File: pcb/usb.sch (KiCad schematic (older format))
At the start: 1 part

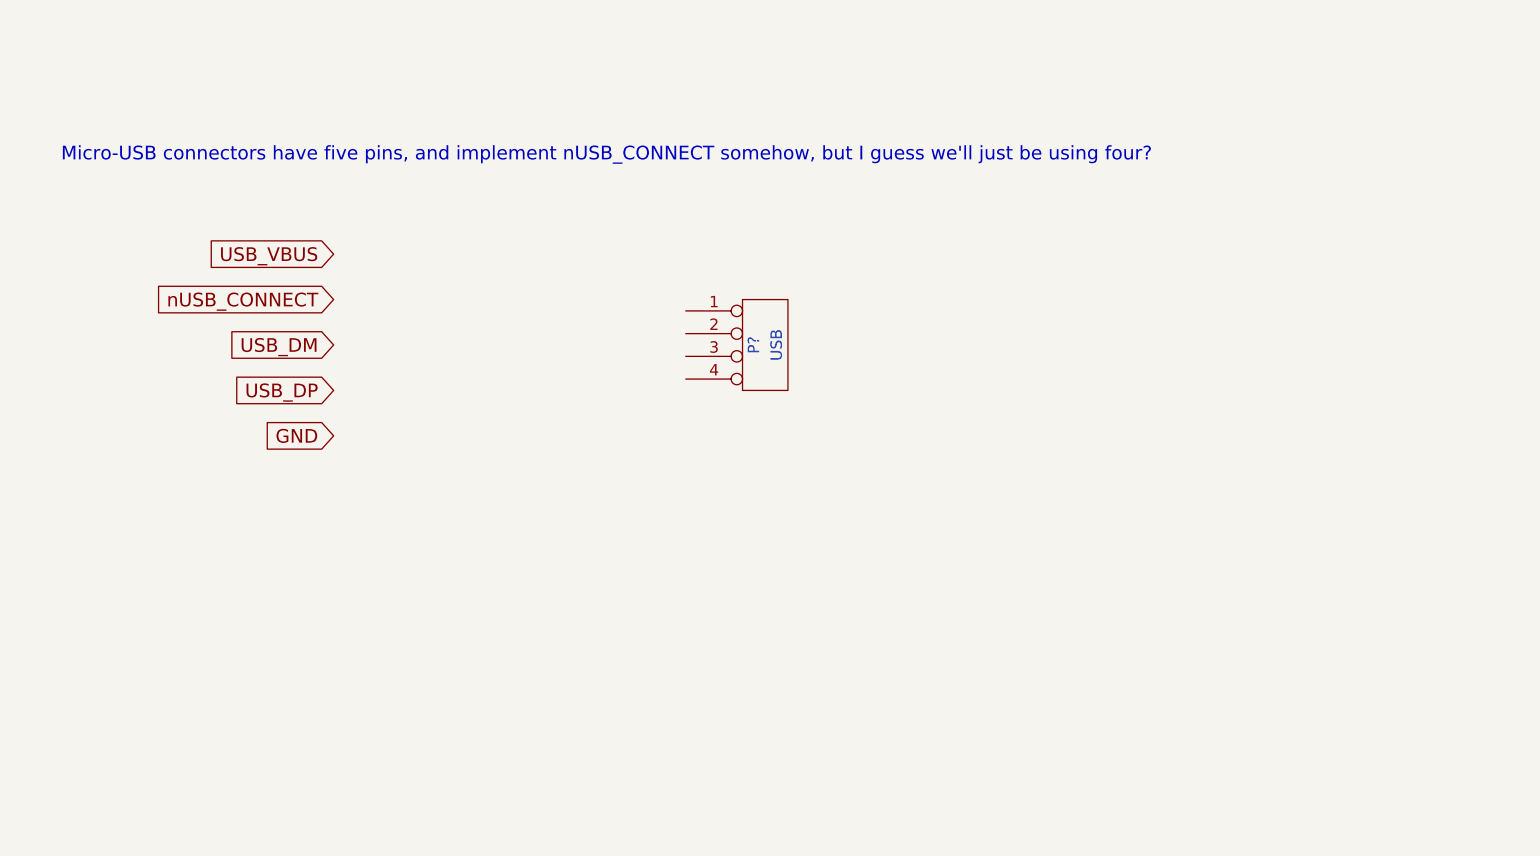
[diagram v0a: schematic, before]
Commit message: added reset pullup, some caps, usb resistors, explanation for nUSB_CONNECT
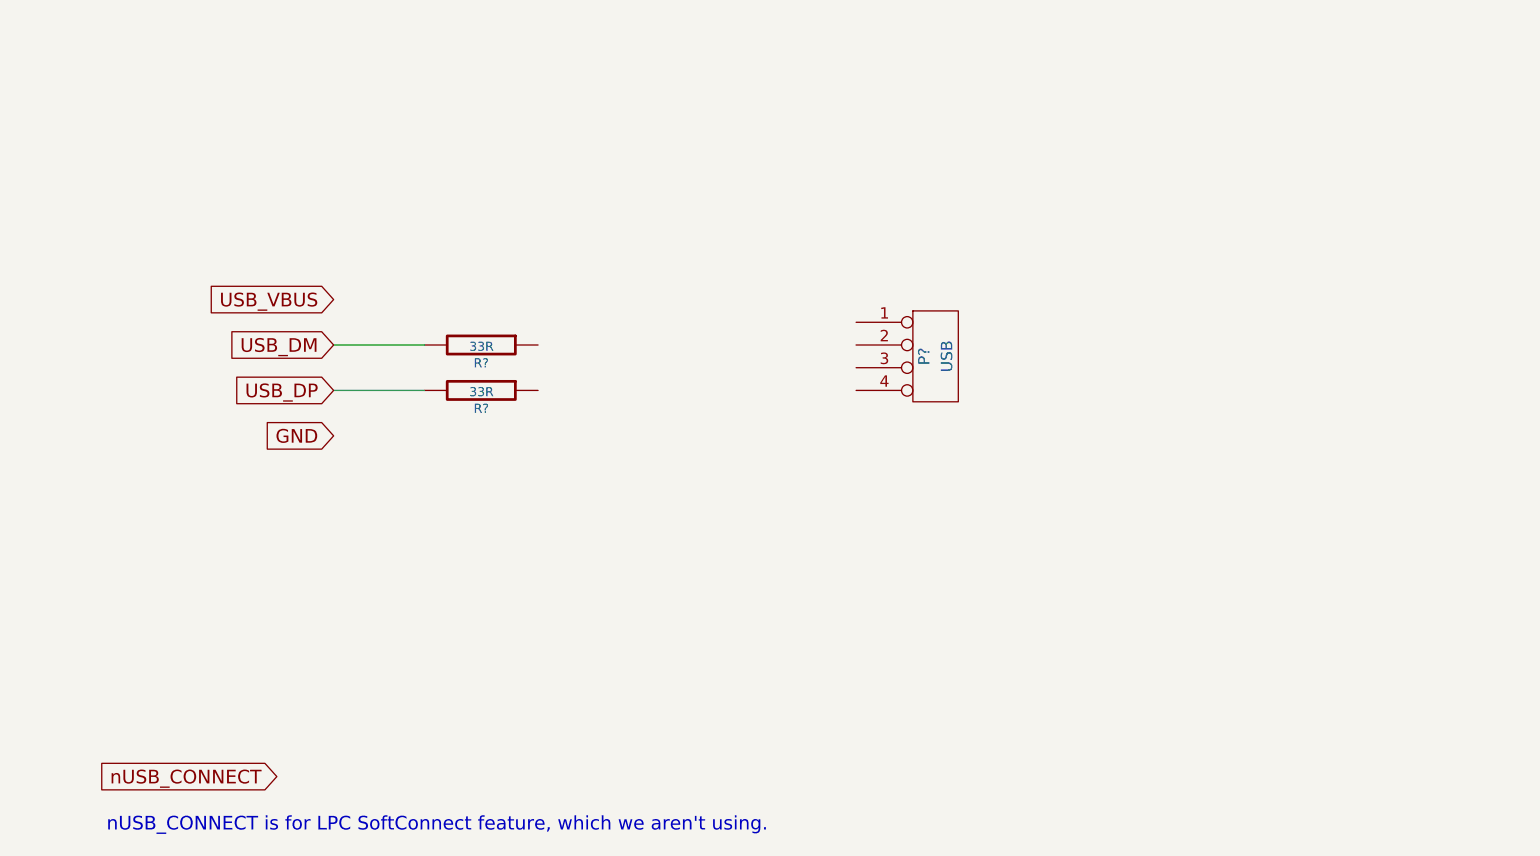
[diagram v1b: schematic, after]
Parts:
- added R? (x2): 33R, ~, symbol R
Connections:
- net USB_DM: now also R?.2
- net USB_DP: now also R?.2
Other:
- note added: "nUSB_CONNECT is for LPC SoftConnect feature, which we aren't using."
- note removed: "Micro-USB connectors have five pins, and implement nUSB_CONNECT somehow, but I guess we'll just be using four?"
- moved on the sheet: P?
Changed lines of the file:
@@
 Comment4 ""
 $EndDescr
-Text GLabel 3750 2600 0    60   Input ~ 0
+Text GLabel 3750 2800 0    60   Input ~ 0
 USB_VBUS
-Text GLabel 3750 2800 0    60   Input ~ 0
+Text GLabel 3500 4900 0    60   Input ~ 0
 nUSB_CONNECT
 Text GLabel 3750 3000 0    60   Input ~ 0
@@
 L CONN_4 P?
 U 1 1 549D55CB
-P 5650 3000
-F 0 "P?" V 5600 3000 50  0000 C CNN
-F 1 "USB" V 5700 3000 50  0000 C CNN
-F 2 "" H 5650 3000 60  0000 C CNN
-F 3 "" H 5650 3000 60  0000 C CNN
-	1    5650 3000
+P 6400 3050
+F 0 "P?" V 6350 3050 50  0000 C CNN
+F 1 "USB" V 6450 3050 50  0000 C CNN
+F 2 "" H 6400 3050 60  0000 C CNN
+F 3 "" H 6400 3050 60  0000 C CNN
+	1    6400 3050
 	1    0    0    -1
 $EndComp
-Text Notes 2550 2200 0    60   ~ 0
-Micro-USB connectors have five pins, and implement nUSB_CONNECT somehow, but I guess we'll just be using four?
+Text Notes 2750 5150 0    60   ~ 0
+nUSB_CONNECT is for LPC SoftConnect feature, which we aren't using.
+$Comp
+L R R?
+U 1 1 549D6477
+P 4400 3000
+F 0 "R?" V 4480 3000 40  0000 C CNN
+F 1 "33R" V 4407 3001 40  0000 C CNN
+F 2 "~" V 4330 3000 30  0000 C CNN
+F 3 "~" H 4400 3000 30  0000 C CNN
+	1    4400 3000
+	0    1    1    0
+$EndComp
+$Comp
+L R R?
+U 1 1 549D6486
+P 4400 3200
+F 0 "R?" V 4480 3200 40  0000 C CNN
+F 1 "33R" V 4407 3201 40  0000 C CNN
+F 2 "~" V 4330 3200 30  0000 C CNN
+F 3 "~" H 4400 3200 30  0000 C CNN
+	1    4400 3200
+	0    1    1    0
+$EndComp
+Wire Wire Line
+	4150 3200 3750 3200
+Wire Wire Line
+	3750 3000 4150 3000
 $EndSCHEMATC

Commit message: thought through power situation a bit more, added some TO DO messages
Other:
- note added: "Probably need to reduce USB_VBUS before it gets to the MCU."
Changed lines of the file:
@@
 Wire Wire Line
 	3750 3000 4150 3000
+Text Notes 2800 2550 0    60   ~ 0
+Probably need to reduce USB_VBUS before it gets to the MCU.
 $EndSCHEMATC

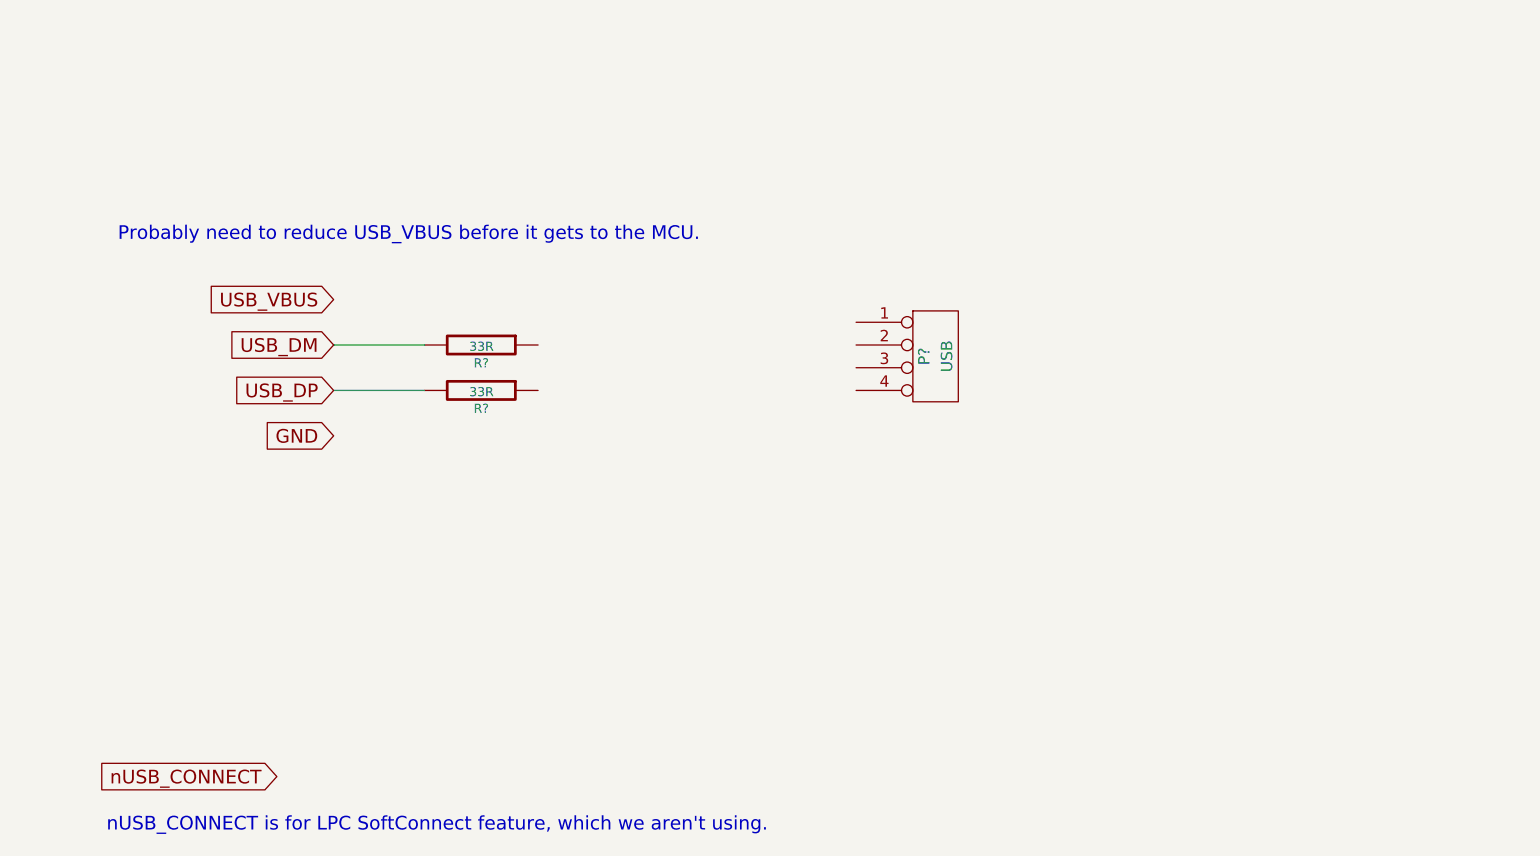
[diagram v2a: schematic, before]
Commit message: made a usb-a plug from usb-if and wikipedia docs
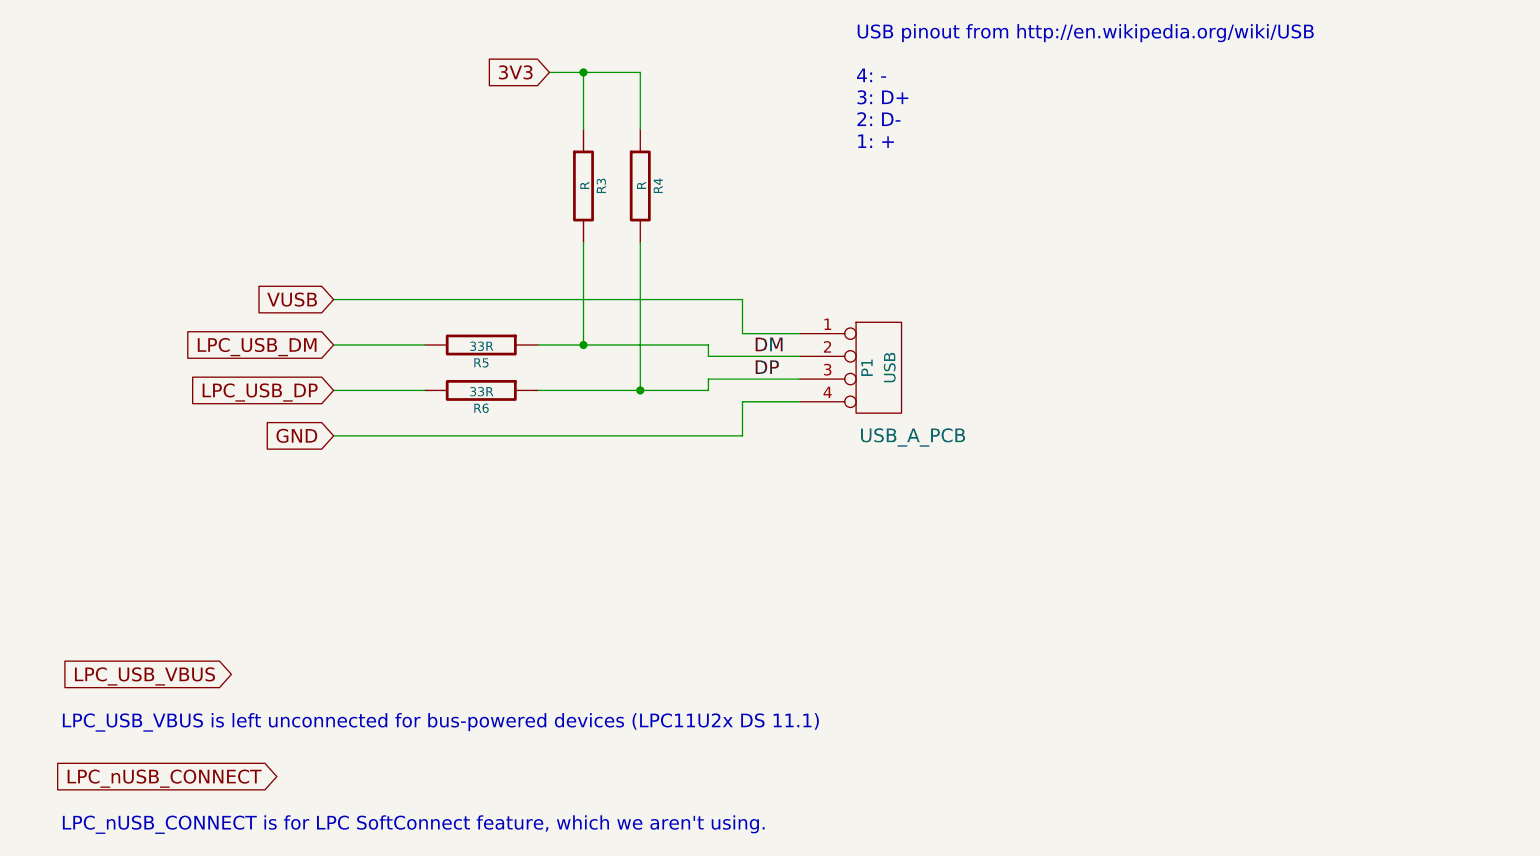
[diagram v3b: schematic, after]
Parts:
- added R3, R4: R, ~, symbol R
- P1: renamed from P?; footprint (none) -> USB_A_PCB
- gave numbers to parts that had none: 2
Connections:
- net GND: now also P1.4 (P4)
- net VUSB: now reaches P1.1 (P1)
- net DM: now reaches P1.2 (P2)
- net DM: now also R5.1, R3.2
- net DP: now reaches P1.3 (P3)
- net DP: now also R6.1, R4.2
- net USB_DM renamed LPC_USB_DM
- net USB_DP renamed LPC_USB_DP
- new net 3V3: R3.1, R4.1
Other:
- note added: "LPC_USB_VBUS is left unconnected for bus-powered devices (LPC11U2x DS 11.1)"
- note added: "LPC_nUSB_CONNECT is for LPC SoftConnect feature, which we aren't using."
- note added: "USB pinout from http://en.wikipedia.org/wiki/USB\n\n4: -\n3: D+\n2: D-\n1: +"
- note removed: "Probably need to reduce USB_VBUS before it gets to the MCU."
- note removed: "nUSB_CONNECT is for LPC SoftConnect feature, which we aren't using."
- moved on the sheet: P1
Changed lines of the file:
@@
 Comment4 ""
 $EndDescr
-Text GLabel 3750 2800 0    60   Input ~ 0
-USB_VBUS
+Text GLabel 3300 4450 0    60   Input ~ 0
+LPC_USB_VBUS
 Text GLabel 3500 4900 0    60   Input ~ 0
-nUSB_CONNECT
+LPC_nUSB_CONNECT
 Text GLabel 3750 3000 0    60   Input ~ 0
-USB_DM
+LPC_USB_DM
 Text GLabel 3750 3200 0    60   Input ~ 0
-USB_DP
+LPC_USB_DP
 Text GLabel 3750 3400 0    60   Input ~ 0
 GND
 $Comp
-L CONN_4 P?
+L CONN_4 P1
 U 1 1 549D55CB
-P 6400 3050
-F 0 "P?" V 6350 3050 50  0000 C CNN
-F 1 "USB" V 6450 3050 50  0000 C CNN
-F 2 "" H 6400 3050 60  0000 C CNN
-F 3 "" H 6400 3050 60  0000 C CNN
-	1    6400 3050
+P 6150 3100
+F 0 "P1" V 6100 3100 50  0000 C CNN
+F 1 "USB" V 6200 3100 50  0000 C CNN
+F 2 "USB_A_PCB" H 6300 2800 60  0000 C CNN
+F 3 "" H 6150 3100 60  0000 C CNN
+	1    6150 3100
 	1    0    0    -1
 $EndComp
-Text Notes 2750 5150 0    60   ~ 0
-nUSB_CONNECT is for LPC SoftConnect feature, which we aren't using.
+Text Notes 2550 5150 0    60   ~ 0
+LPC_nUSB_CONNECT is for LPC SoftConnect feature, which we aren't using.
 $Comp
-L R R?
+L R R5
 U 1 1 549D6477
 P 4400 3000
-F 0 "R?" V 4480 3000 40  0000 C CNN
+F 0 "R5" V 4480 3000 40  0000 C CNN
 F 1 "33R" V 4407 3001 40  0000 C CNN
 F 2 "~" V 4330 3000 30  0000 C CNN
@@
 $EndComp
 $Comp
-L R R?
+L R R6
 U 1 1 549D6486
 P 4400 3200
-F 0 "R?" V 4480 3200 40  0000 C CNN
+F 0 "R6" V 4480 3200 40  0000 C CNN
 F 1 "33R" V 4407 3201 40  0000 C CNN
 F 2 "~" V 4330 3200 30  0000 C CNN
@@
 Wire Wire Line
 	3750 3000 4150 3000
-Text Notes 2800 2550 0    60   ~ 0
-Probably need to reduce USB_VBUS before it gets to the MCU.
+Text GLabel 3750 2800 0    60   Input ~ 0
+VUSB
+Text Notes 2550 4700 0    60   ~ 0
+LPC_USB_VBUS is left unconnected for bus-powered devices (LPC11U2x DS 11.1)
+$Comp
+L R R3
+U 1 1 549DD948
+P 4850 2300
+F 0 "R3" V 4930 2300 40  0000 C CNN
+F 1 "R" V 4857 2301 40  0000 C CNN
+F 2 "~" V 4780 2300 30  0000 C CNN
+F 3 "~" H 4850 2300 30  0000 C CNN
+	1    4850 2300
+	1    0    0    -1
+$EndComp
+$Comp
+L R R4
+U 1 1 549DD957
+P 5100 2300
+F 0 "R4" V 5180 2300 40  0000 C CNN
+F 1 "R" V 5107 2301 40  0000 C CNN
+F 2 "~" V 5030 2300 30  0000 C CNN
+F 3 "~" H 5100 2300 30  0000 C CNN
+	1    5100 2300
+	1    0    0    -1
+$EndComp
+Text GLabel 4700 1800 0    60   Input ~ 0
+3V3
+Wire Wire Line
+	4700 1800 5100 1800
+Wire Wire Line
+	4850 1800 4850 2050
+Wire Wire Line
+	5100 1800 5100 2050
+Connection ~ 4850 1800
+Wire Wire Line
+	4650 3000 5400 3000
+Wire Wire Line
+	4850 3000 4850 2550
+Wire Wire Line
+	4650 3200 5400 3200
+Wire Wire Line
+	5100 3200 5100 2550
+Wire Wire Line
+	5400 3000 5400 3050
+Wire Wire Line
+	5400 3050 5800 3050
+Connection ~ 4850 3000
+Wire Wire Line
+	5400 3200 5400 3150
+Wire Wire Line
+	5400 3150 5800 3150
+Connection ~ 5100 3200
+Wire Wire Line
+	3750 3400 5550 3400
+Wire Wire Line
+	5550 3400 5550 3250
+Wire Wire Line
+	5550 3250 5800 3250
+Wire Wire Line
+	5800 2950 5550 2950
+Wire Wire Line
+	5550 2950 5550 2800
+Wire Wire Line
+	5550 2800 3750 2800
+Text Notes 6050 2150 0    60   ~ 0
+USB pinout from http://en.wikipedia.org/wiki/USB\n\n4: -\n3: D+\n2: D-\n1: +
+Text Label 5600 3050 0    60   ~ 0
+DM
+Text Label 5600 3150 0    60   ~ 0
+DP
 $EndSCHEMATC

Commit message: power and usb - a bit more progress
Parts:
- added C8, C9: 47p, ~, symbol C
- R3: value R -> 1k5 LS
- R4: value R -> 1k5 FS
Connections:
- net DM: now also C8.1
- net DP: now also C9.1
- net GND: now also C8.2, C9.2
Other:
- note added: "Populate R3 (1k5 LS) for low-speed USB\nor R4 (1k5 FS) for full/high-speed USB."
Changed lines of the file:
@@
 P 4850 2300
 F 0 "R3" V 4930 2300 40  0000 C CNN
-F 1 "R" V 4857 2301 40  0000 C CNN
+F 1 "1k5 LS" V 4857 2301 40  0000 C CNN
 F 2 "~" V 4780 2300 30  0000 C CNN
 F 3 "~" H 4850 2300 30  0000 C CNN
@@
 P 5100 2300
 F 0 "R4" V 5180 2300 40  0000 C CNN
-F 1 "R" V 5107 2301 40  0000 C CNN
+F 1 "1k5 FS" V 5107 2301 40  0000 C CNN
 F 2 "~" V 5030 2300 30  0000 C CNN
 F 3 "~" H 5100 2300 30  0000 C CNN
@@
 	4650 3000 5400 3000
 Wire Wire Line
-	4850 3000 4850 2550
+	4850 2550 4850 3300
 Wire Wire Line
 	4650 3200 5400 3200
 Wire Wire Line
-	5100 3200 5100 2550
+	5100 2550 5100 3300
 Wire Wire Line
 	5400 3000 5400 3050
@@
 	5400 3150 5800 3150
 Connection ~ 5100 3200
-Wire Wire Line
-	3750 3400 5550 3400
-Wire Wire Line
-	5550 3400 5550 3250
 Wire Wire Line
 	5550 3250 5800 3250
@@
 Text Label 5600 3150 0    60   ~ 0
 DP
+$Comp
+L C C9
+U 1 1 549E778E
+P 5100 3500
+F 0 "C9" H 5100 3600 40  0000 L CNN
+F 1 "47p" H 5106 3415 40  0000 L CNN
+F 2 "~" H 5138 3350 30  0000 C CNN
+F 3 "~" H 5100 3500 60  0000 C CNN
+	1    5100 3500
+	1    0    0    -1
+$EndComp
+$Comp
+L C C8
+U 1 1 549E779B
+P 4850 3500
+F 0 "C8" H 4850 3600 40  0000 L CNN
+F 1 "47p" H 4856 3415 40  0000 L CNN
+F 2 "~" H 4888 3350 30  0000 C CNN
+F 3 "~" H 4850 3500 60  0000 C CNN
+	1    4850 3500
+	1    0    0    -1
+$EndComp
+Wire Wire Line
+	5550 3700 5550 3250
+Connection ~ 5100 3700
+Connection ~ 4850 3700
+Wire Wire Line
+	3750 3400 4050 3400
+Wire Wire Line
+	4050 3400 4050 3700
+Wire Wire Line
+	4050 3700 5550 3700
+Text Notes 2800 2250 0    60   ~ 0
+Populate R3 (1k5 LS) for low-speed USB\nor R4 (1k5 FS) for full/high-speed USB.
 $EndSCHEMATC
